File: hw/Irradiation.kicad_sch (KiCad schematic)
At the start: 12 parts, among them U19 WS2812B, U20 WS2812B, U21 WS2812B, U22 WS2812B, U23 WS2812B, U24 WS2812B

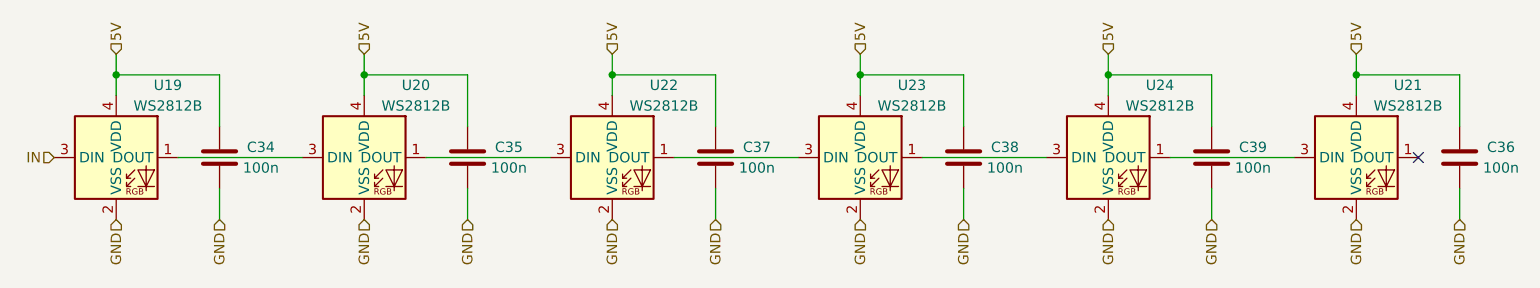
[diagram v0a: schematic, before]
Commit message: D7 and bigger vias
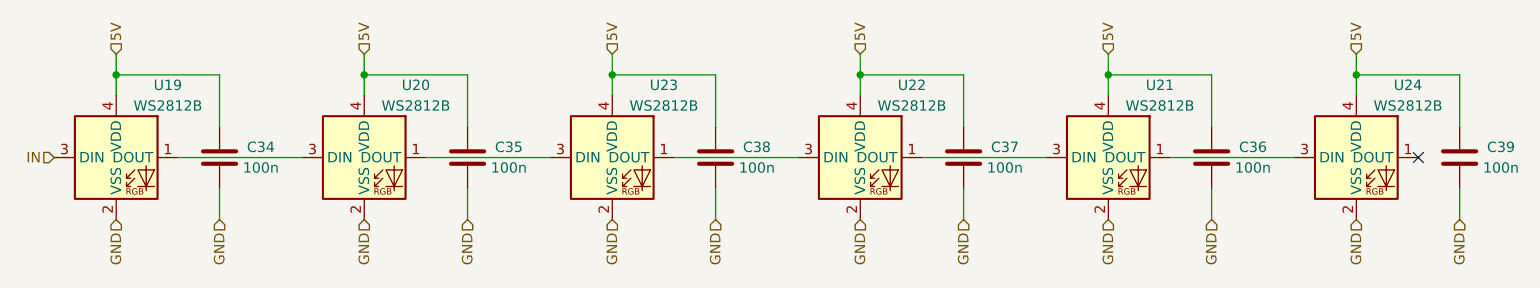
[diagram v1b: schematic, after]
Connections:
- net at U20.1 (DOUT): now also U23.3 (DIN); no longer U22.3 (DIN)
- net at U24.1 (DOUT): no longer U21.3 (DIN)
- net at U24.3 (DIN): now also U21.1 (DOUT); no longer U23.1 (DOUT)
- net at U22.1 (DOUT): now also U21.3 (DIN); no longer U23.3 (DIN)
- new net: U22.3 (DIN), U23.1 (DOUT)
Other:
- moved on the sheet: C36, C37, C38, C39, U21, U22, U23, U24
